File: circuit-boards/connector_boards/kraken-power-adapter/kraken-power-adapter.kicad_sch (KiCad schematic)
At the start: 13 parts, among them J1 Vbat+, J2 Vbat-, J3 Vbat PP15-45, J4 PP15/45-HOUSING W/SPG-RED, J5 PP15/45-HOUSING W/SPG-BLACK, J6 PP15/45 PCB Vertical Pin, J7 PP15/45 PCB Vertical Pin

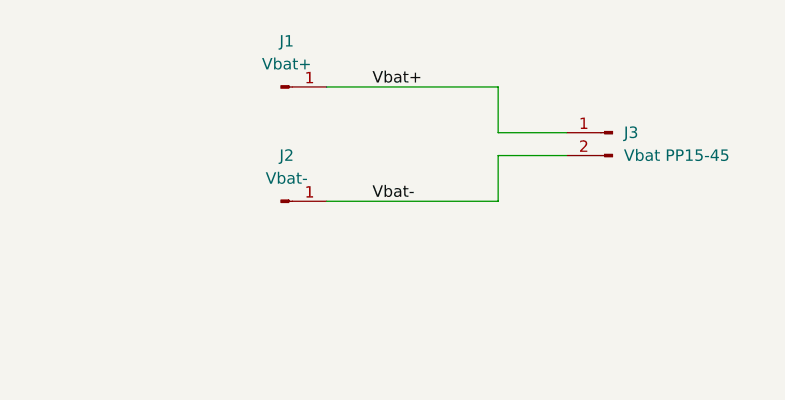
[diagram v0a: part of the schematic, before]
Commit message: Modified kraken power to rotate andersons 90 deg
Signed-off-by: Scott Berman <sgberman1@gmail.com>
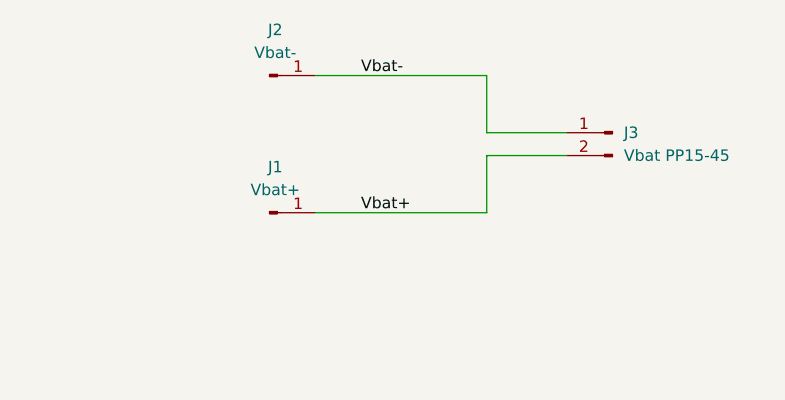
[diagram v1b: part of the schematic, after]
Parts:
- J3: footprint kraken-adapter:Dual-stacked-1335G1 -> kraken-adapter:Dual-side-by-side-1335G1
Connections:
- net Vbat+: now also J3.2 (Pin_2); no longer J3.1 (Pin_1)
- net Vbat-: now also J3.1 (Pin_1); no longer J3.2 (Pin_2)
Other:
- moved on the sheet: J1, J2
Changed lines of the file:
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@@
     (company "971 Spartan Robotics")
   )
-  (wire (pts (xy 151.13 72.39) (xy 143.51 72.39))
-    (stroke (width 0) (type default))
-  )
-  (wire (pts (xy 124.46 64.77) (xy 143.51 64.77))
-    (stroke (width 0) (type default))
-  )
-  (wire (pts (xy 151.13 69.85) (xy 143.51 69.85))
-    (stroke (width 0) (type default))
-  )
-  (wire (pts (xy 124.46 77.47) (xy 143.51 77.47))
-    (stroke (width 0) (type default))
-  )
-  (wire (pts (xy 143.51 69.85) (xy 143.51 64.77))
-    (stroke (width 0) (type default))
-  )
-  (wire (pts (xy 143.51 72.39) (xy 143.51 77.47))
-    (stroke (width 0) (type default))
-  )
-  (label "Vbat+" (at 129.54 64.77 0) (fields_autoplaced)
+  (wire (pts (xy 142.24 78.74) (xy 142.24 72.39))
+    (stroke (width 0) (type default))
+  )
+  (wire (pts (xy 142.24 69.85) (xy 151.13 69.85))
+    (stroke (width 0) (type default))
+  )
+  (wire (pts (xy 142.24 63.5) (xy 142.24 69.85))
+    (stroke (width 0) (type default))
+  )
+  (wire (pts (xy 123.19 78.74) (xy 142.24 78.74))
+    (stroke (width 0) (type default))
+  )
+  (wire (pts (xy 142.24 72.39) (xy 151.13 72.39))
+    (stroke (width 0) (type default))
+  )
+  (wire (pts (xy 123.19 63.5) (xy 142.24 63.5))
+    (stroke (width 0) (type default))
+  )
+  (label "Vbat+" (at 128.27 78.74 0) (fields_autoplaced)
     (effects (font (size 1.27 1.27)) (justify left bottom))
   )
-  (label "Vbat-" (at 129.54 77.47 0) (fields_autoplaced)
+  (label "Vbat-" (at 128.27 63.5 0) (fields_autoplaced)
     (effects (font (size 1.27 1.27)) (justify left bottom))
   )
@@
     )
   )
-  (symbol (lib_id "Connector:Conn_01x01_Pin") (at 119.38 77.47 0) (unit 1)
-    (in_bom no) (on_board yes) (dnp no) (fields_autoplaced)
-    (property "Reference" "J2" (at 120.015 72.39 0)
-      (effects (font (size 1.27 1.27)))
-    )
-    (property "Value" "Vbat-" (at 120.015 74.93 0)
-      (effects (font (size 1.27 1.27)))
-    )
-    (property "Footprint" "kraken-adapter:ScrewTerminal-#6" (at 119.38 77.47 0)
-      (effects (font (size 1.27 1.27)) hide)
-    )
-    (property "Datasheet" "~" (at 119.38 77.47 0)
-      (effects (font (size 1.27 1.27)) hide)
-    )
-    (property "MFG" "" (at 119.38 77.47 0)
-      (effects (font (size 1.27 1.27)) hide)
-    )
-    (property "MFG P/N" "" (at 119.38 77.47 0)
-      (effects (font (size 1.27 1.27)) hide)
-    )
-    (property "DIST" "" (at 119.38 77.47 0)
-      (effects (font (size 1.27 1.27)) hide)
-    )
-    (property "DIST P/N" "" (at 119.38 77.47 0)
+  (symbol (lib_id "Connector:Conn_01x01_Pin") (at 118.11 63.5 0) (unit 1)
+    (in_bom no) (on_board yes) (dnp no) (fields_autoplaced)
+    (property "Reference" "J2" (at 118.745 58.42 0)
+      (effects (font (size 1.27 1.27)))
+    )
+    (property "Value" "Vbat-" (at 118.745 60.96 0)
+      (effects (font (size 1.27 1.27)))
+    )
+    (property "Footprint" "kraken-adapter:ScrewTerminal-#6" (at 118.11 63.5 0)
+      (effects (font (size 1.27 1.27)) hide)
+    )
+    (property "Datasheet" "~" (at 118.11 63.5 0)
+      (effects (font (size 1.27 1.27)) hide)
+    )
+    (property "MFG" "" (at 118.11 63.5 0)
+      (effects (font (size 1.27 1.27)) hide)
+    )
+    (property "MFG P/N" "" (at 118.11 63.5 0)
+      (effects (font (size 1.27 1.27)) hide)
+    )
+    (property "DIST" "" (at 118.11 63.5 0)
+      (effects (font (size 1.27 1.27)) hide)
+    )
+    (property "DIST P/N" "" (at 118.11 63.5 0)
       (effects (font (size 1.27 1.27)) hide)
     )
@@
     )
   )
-  (symbol (lib_id "Connector:Conn_01x01_Pin") (at 119.38 64.77 0) (unit 1)
-    (in_bom no) (on_board yes) (dnp no) (fields_autoplaced)
-    (property "Reference" "J1" (at 120.015 59.69 0)
-      (effects (font (size 1.27 1.27)))
-    )
-    (property "Value" "Vbat+" (at 120.015 62.23 0)
-      (effects (font (size 1.27 1.27)))
-    )
-    (property "Footprint" "kraken-adapter:ScrewTerminal-#6" (at 119.38 64.77 0)
-      (effects (font (size 1.27 1.27)) hide)
-    )
-    (property "Datasheet" "~" (at 119.38 64.77 0)
-      (effects (font (size 1.27 1.27)) hide)
-    )
-    (property "MFG" "" (at 119.38 64.77 0)
-      (effects (font (size 1.27 1.27)) hide)
-    )
-    (property "MFG P/N" "" (at 119.38 64.77 0)
-      (effects (font (size 1.27 1.27)) hide)
-    )
-    (property "DIST" "" (at 119.38 64.77 0)
-      (effects (font (size 1.27 1.27)) hide)
-    )
-    (property "DIST P/N" "" (at 119.38 64.77 0)
+  (symbol (lib_id "Connector:Conn_01x01_Pin") (at 118.11 78.74 0) (unit 1)
+    (in_bom no) (on_board yes) (dnp no) (fields_autoplaced)
+    (property "Reference" "J1" (at 118.745 73.66 0)
+      (effects (font (size 1.27 1.27)))
+    )
+    (property "Value" "Vbat+" (at 118.745 76.2 0)
+      (effects (font (size 1.27 1.27)))
+    )
+    (property "Footprint" "kraken-adapter:ScrewTerminal-#6" (at 118.11 78.74 0)
+      (effects (font (size 1.27 1.27)) hide)
+    )
+    (property "Datasheet" "~" (at 118.11 78.74 0)
+      (effects (font (size 1.27 1.27)) hide)
+    )
+    (property "MFG" "" (at 118.11 78.74 0)
+      (effects (font (size 1.27 1.27)) hide)
+    )
+    (property "MFG P/N" "" (at 118.11 78.74 0)
+      (effects (font (size 1.27 1.27)) hide)
+    )
+    (property "DIST" "" (at 118.11 78.74 0)
+      (effects (font (size 1.27 1.27)) hide)
+    )
+    (property "DIST P/N" "" (at 118.11 78.74 0)
       (effects (font (size 1.27 1.27)) hide)
     )
@@
       (effects (font (size 1.27 1.27)) (justify right))
     )
-    (property "Footprint" "kraken-adapter:Dual-stacked-1335G1" (at 156.21 69.85 0)
-      (effects (font (size 1.27 1.27)) hide)
-    )
+    (property "Footprint" "kraken-adapter:Dual-side-by-side-1335G1" (at 156.21 69.85 0)
+      (effects (font (size 1.27 1.27)) hide)
+    )
